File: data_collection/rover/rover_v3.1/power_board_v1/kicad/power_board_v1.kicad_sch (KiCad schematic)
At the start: 96 parts, among them J1 XT60_BATT, J10 from Pi USB2, J11 UPDI prog (UPDI/3V3/GND), J12 XT30 fallback pads, J2 PANEL_SW, J3 USB-C PWR OUT (TH shell), J4 USB_A radio1, J5 USB_A radio2, J6 AUX 5V 2A, J7 PI GPIO harness, J8 AUX_CTL out (JST-GH), J9 from Pi USB1, Q2 SQJQ140E-A diode, Q3 SQJQ140E-B switch, U1 LM25145 5.1V rail A, U2 LM25145 5.1V rail B, U3 ATtiny816, U4 LM74800-Q1, U5 INA226 (addr 0x40), U6 TPS7A16 3V3 60V LDO, U7 TPS2553 1.7A, U8 TPS2553 1.7A, U9 AP2112K-3.3 (switched)

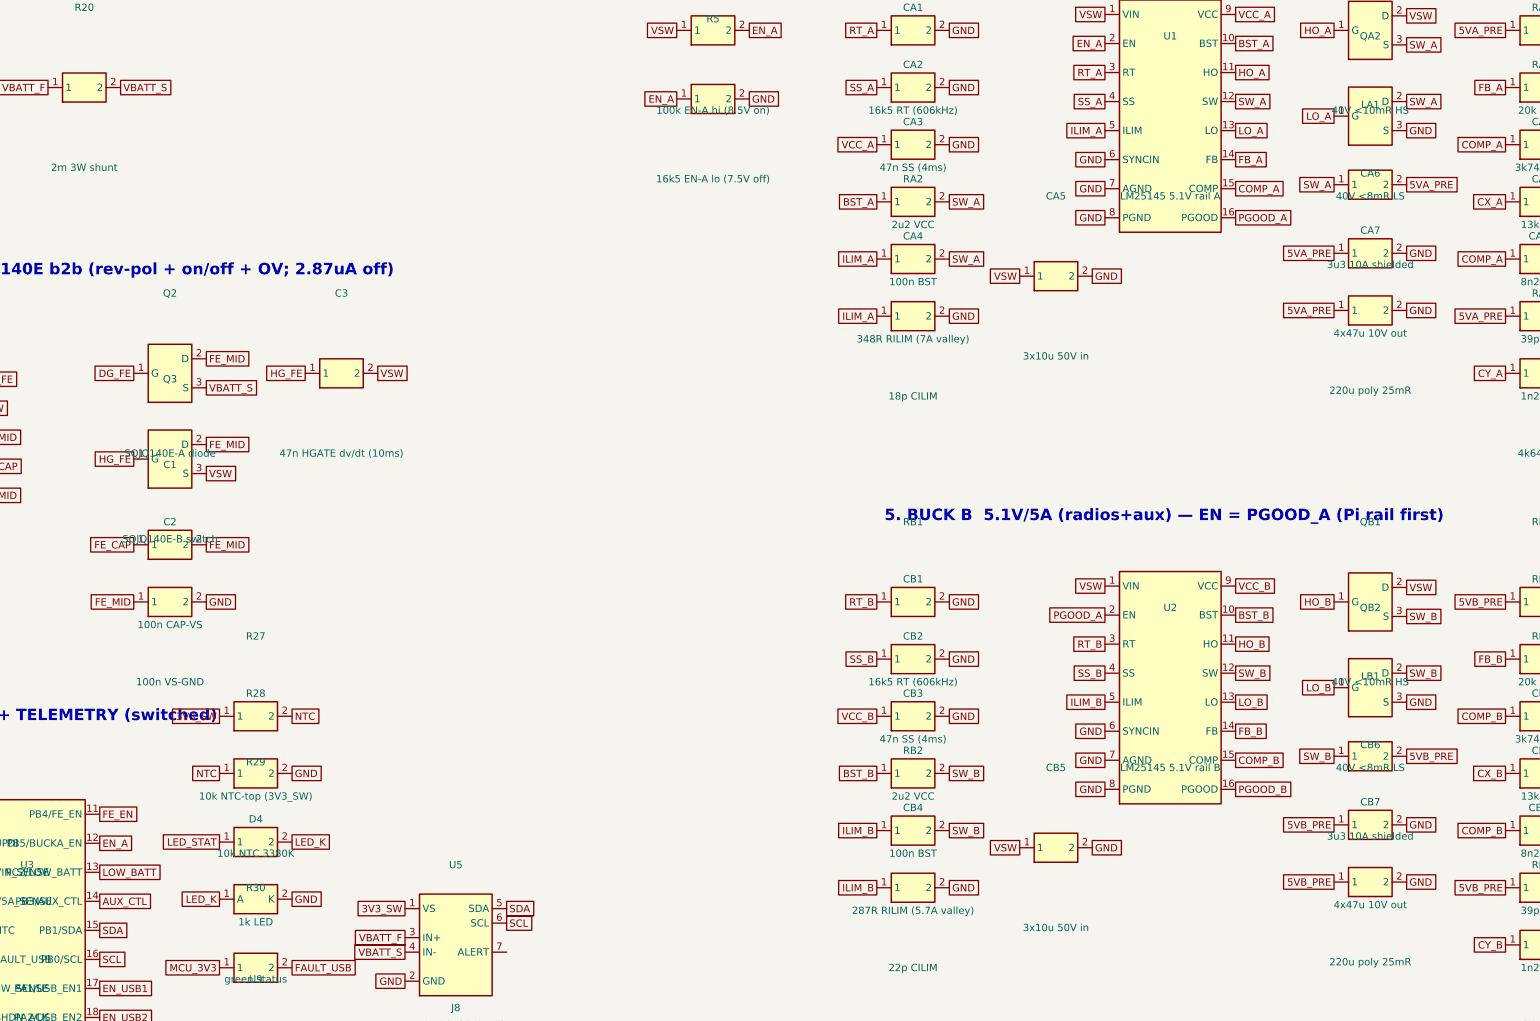
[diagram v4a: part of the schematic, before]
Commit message: P2 BOM lockdown: all lines LCSC-verified w/ C#s; subs LM25145->LM5145 (eq-identical, verified), SQJQ140E->2x CSD18543Q3A, tiny816 SOIC->UQFN; RILIM 301/243; schematic regenerated; ~$43/board @5
Co-Authored-By: Claude Fable 5 <noreply@anthropic.com>
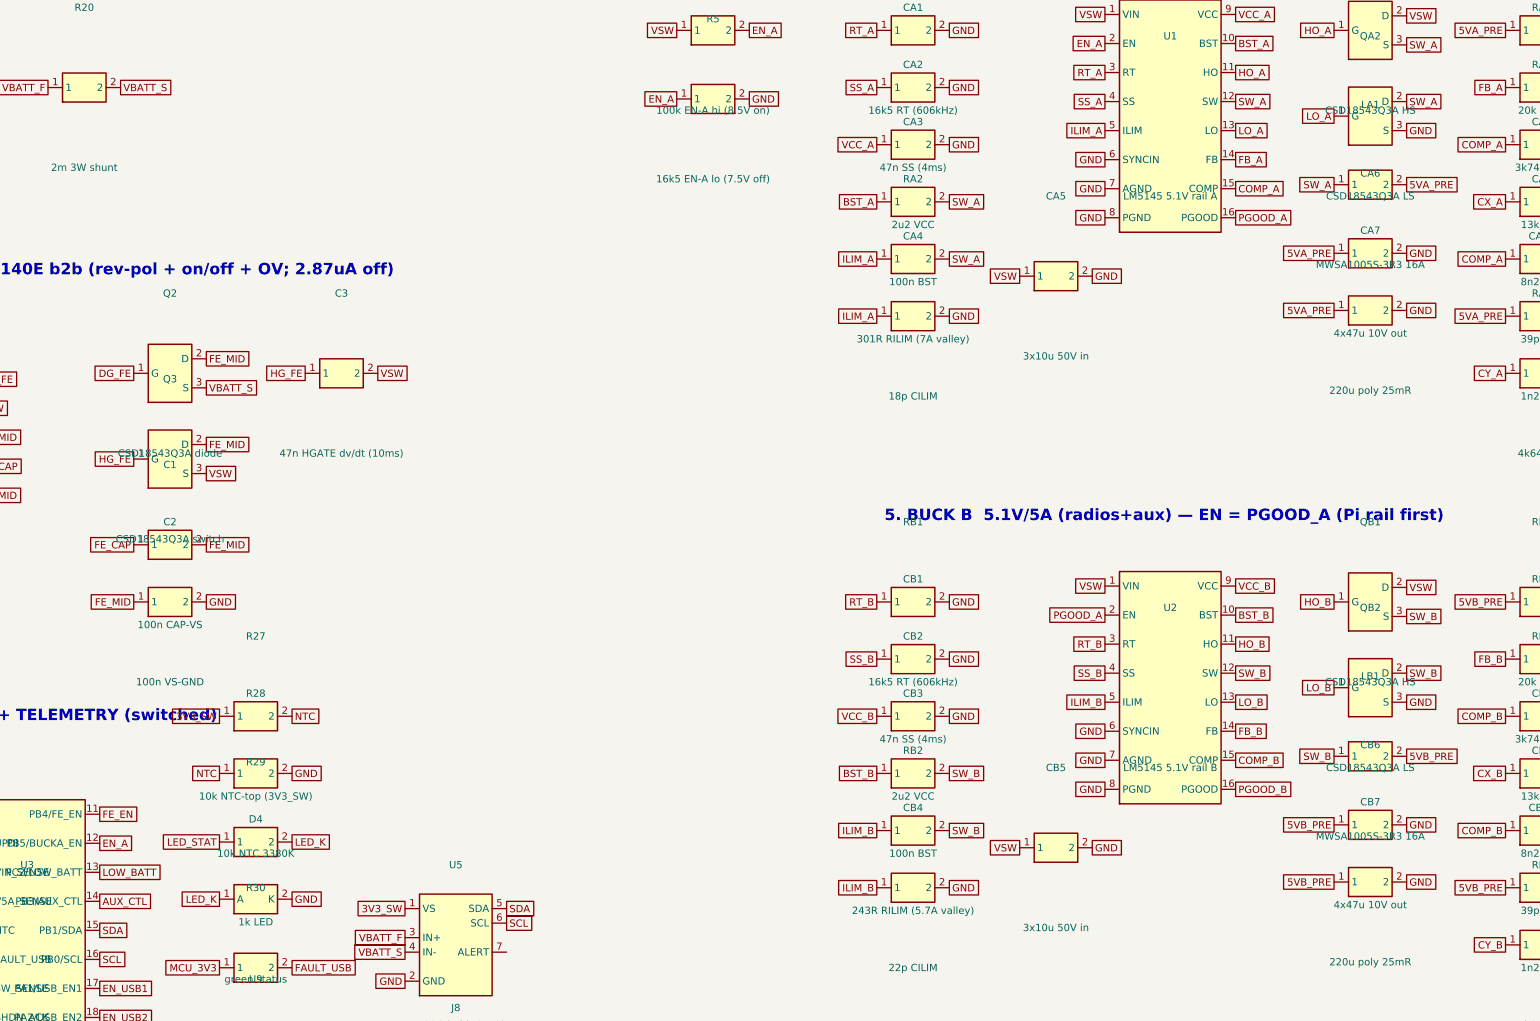
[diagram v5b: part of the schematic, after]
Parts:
- removed U1: LM25145 5.1V rail A, symbol pwr:LM25145
- removed U2: LM25145 5.1V rail B, symbol pwr:LM25145
- added U1: LM5145 5.1V rail A, symbol pwr:LM5145
- added U2: LM5145 5.1V rail B, symbol pwr:LM5145
- LA1, LB1: value 3u3 10A shielded -> MWSA1005S-3R3 16A
- Q2: value SQJQ140E-A diode -> CSD18543Q3A diode
- Q3: value SQJQ140E-B switch -> CSD18543Q3A switch
- QA1, QB1: value 40V <10mR HS -> CSD18543Q3A HS
- QA2, QB2: value 40V <8mR LS -> CSD18543Q3A LS
- RA2: value 348R RILIM (7A valley) -> 301R RILIM (7A valley)
- RB2: value 287R RILIM (5.7A valley) -> 243R RILIM (5.7A valley)
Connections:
- net BST_A: now also U1.10 (BST)
- net BST_B: now also U2.10 (BST)
- net COMP_A: now also U1.15 (COMP)
- net COMP_B: now also U2.15 (COMP)
- net EN_A: now also U1.2 (EN)
- net FB_A: now also U1.14 (FB)
- net FB_B: now also U2.14 (FB)
- net GND: now also U1.6 (SYNCIN), U1.7 (AGND), U1.8 (PGND), U2.6 (SYNCIN), U2.7 (AGND), U2.8 (PGND)
- net HO_A: now also U1.11 (HO)
- net HO_B: now also U2.11 (HO)
- net ILIM_A: now also U1.5 (ILIM)
- net ILIM_B: now also U2.5 (ILIM)
- net LO_A: now also U1.13 (LO)
- net LO_B: now also U2.13 (LO)
- net PGOOD_A: now also U1.16 (PGOOD), U2.2 (EN)
- net PGOOD_B: now also U2.16 (PGOOD)
- net RT_A: now also U1.3 (RT)
- net RT_B: now also U2.3 (RT)
- net SS_A: now also U1.4 (SS)
- net SS_B: now also U2.4 (SS)
- net SW_A: now also U1.12 (SW)
- net SW_B: now also U2.12 (SW)
- net VCC_A: now also U1.9 (VCC)
- net VCC_B: now also U2.9 (VCC)
- net VSW: now also U1.1 (VIN), U2.1 (VIN)

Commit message: P3 prep: FOOTPRINTS.md (land patterns + 90x65 floorplan zones); KiCad-7 dialect emit; schematic PDF export + PNG-verified collision fixes (per-height ref/value offsets, ATtiny width, stale SQJQ140E title); netlist audit clean (73 nets)
Co-Authored-By: Claude Fable 5 <noreply@anthropic.com>
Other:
- note added: "2. FRONT-END: LM74800-Q1 + 2x CSD18543Q3A b2b (rev-pol + on/off + OV; 2.87uA off)"
- note removed: "2. FRONT-END: LM74800-Q1 + SQJQ140E b2b (rev-pol + on/off + OV; 2.87uA off)"

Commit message: Schematic v3: physical package pads throughout (datasheet-verified pinouts for LM5145 RGY, ATtiny816 VQFN, INA226, TPS2553, TPS7A16, AP2112K, CSD18543Q3A); netlist 86 nets clean; 18 pad spot-checks pass; PNG-verified
Co-Authored-By: Claude Fable 5 <noreply@anthropic.com>
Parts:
- removed Q2: CSD18543Q3A diode, symbol pwr:NFET
- removed Q3: CSD18543Q3A switch, symbol pwr:NFET
- removed QA1, QB1: CSD18543Q3A HS, symbol pwr:NFET
- removed QA2, QB2: CSD18543Q3A LS, symbol pwr:NFET
- removed U6: TPS7A16 3V3 60V LDO, symbol pwr:LDO
- removed U9: AP2112K-3.3 (switched), symbol pwr:LDO
- added Q2: CSD18543Q3A diode, symbol pwr:NFET_SON
- added Q3: CSD18543Q3A switch, symbol pwr:NFET_SON
- added QA1, QB1: CSD18543Q3A HS, symbol pwr:NFET_SON
- added QA2, QB2: CSD18543Q3A LS, symbol pwr:NFET_SON
- added U6: TPS7A1633 3V3 60V LDO, symbol pwr:TPS7A16
- added U9: AP2112K-3.3 (switched), symbol pwr:AP2112
- U3: value ATtiny816 -> ATtiny816 (VQFN)
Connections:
- net 3V3_SW: now also U5.6 (VS), U9.5 (VOUT); no longer U5.1 (VS)
- net 5V_B: now also U9.1 (VIN), U9.3 (EN)
- net AUX_CTL: now also U3.11 (PB3/AUX_CTL); no longer U3.14 (PB3/AUX_CTL)
- net BST_A: now also U1.17 (BST); no longer U1.10 (BST)
- net BST_B: now also U2.17 (BST); no longer U2.10 (BST)
- net COMP_A: now also U1.4 (COMP); no longer U1.15 (COMP)
- net COMP_B: now also U2.4 (COMP); no longer U2.15 (COMP)
- net DG_FE: now also Q2.4 (G)
- net EN_A: now also U1.1 (EN), U3.9 (PB5/BUCKA_EN); no longer U1.2 (EN), U3.12 (PB5/BUCKA_EN)
- net EN_USB1: now also U3.20 (PA1/USB_EN1), U7.3 (EN); no longer U3.17 (PA1/USB_EN1), U7.2 (EN)
- net EN_USB2: now also U3.1 (PA2/USB_EN2), U8.3 (EN); no longer U3.18 (PA2/USB_EN2), U8.2 (EN)
- net FAULT_USB: now also U3.6 (PA5/FAULT_USB), U7.4 (FAULT), U8.4 (FAULT); no longer U3.7 (PA5/FAULT_USB), U7.5 (FAULT), U8.5 (FAULT)
- net FB_A: now also U1.5 (FB); no longer U1.14 (FB)
- net FB_B: now also U2.5 (FB); no longer U2.14 (FB)
- net FE_EN: now also U3.10 (PB4/FE_EN); no longer U3.11 (PB4/FE_EN)
- net FE_MID: now also Q2.5 (D), Q2.6 (D), Q2.7 (D), Q2.8 (D), Q3.5 (D), Q3.6 (D), Q3.7 (D), Q3.8 (D)
- net GND: now also U1.12 (PGND), U1.21 (EP), U2.12 (PGND), U2.21 (EP), U3.3 (GND), U5.1 (A1), U5.7 (GND), U7.2 (GND), U8.2 (GND), QA2.1 (S), QA2.2 (S), QA2.3 (S), QB2.1 (S), QB2.2 (S), QB2.3 (S), U6.4 (GND), U6.9 (PAD), U9.2 (GND); no longer U1.7 (AGND), U2.7 (AGND), U3.2 (GND), U7.3 (GND), U8.3 (GND)
- net HG_FE: now also Q3.4 (G)
- net HO_A: now also U1.18 (HO), QA1.4 (G); no longer U1.11 (HO)
- net HO_B: now also U2.18 (HO), QB1.4 (G); no longer U2.11 (HO)
- net ILIM1: now also U7.5 (ILIM); no longer U7.6 (ILIM)
- net ILIM2: now also U8.5 (ILIM); no longer U8.6 (ILIM)
- net ILIM_A: now also U1.11 (ILIM); no longer U1.5 (ILIM)
- net ILIM_B: now also U2.11 (ILIM); no longer U2.5 (ILIM)
- net LED_STAT: now also U3.2 (PA3/LED); no longer U3.19 (PA3/LED)
- net LOW_BATT: now also U3.17 (PC2/LOW_BATT); no longer U3.13 (PC2/LOW_BATT)
- net LO_A: now also QA2.4 (G)
- net LO_B: now also QB2.4 (G)
- net MCU_3V3: now also U3.4 (VDD), U6.1 (OUT); no longer U3.1 (VCC)
- net NTC: now also U3.8 (PA7/NTC); no longer U3.6 (PA7/NTC)
- net PGOOD_A: now also U1.10 (PGOOD), U2.1 (EN), U3.15 (PC0/PGOOD_A); no longer U1.16 (PGOOD), U2.2 (EN), U3.10 (PC0/PGOOD_A)
- net PGOOD_B: now also U2.10 (PGOOD), U3.16 (PC1/PGOOD_B); no longer U2.16 (PGOOD), U3.20 (PC1/PGOOD_B)
- net RT_A: now also U1.2 (RT); no longer U1.3 (RT)
- net RT_B: now also U2.2 (RT); no longer U2.3 (RT)
- net SCL: now also U3.14 (PB0/SCL), U5.5 (SCL); no longer U3.16 (PB0/SCL), U5.6 (SCL)
- net SDA: now also U3.13 (PB1/SDA), U5.4 (SDA); no longer U3.15 (PB1/SDA), U5.5 (SDA)
- net SHDN_ACK: now also U3.18 (PC3/SHDN_ACK); no longer U3.9 (PC3/SHDN_ACK)
- net SS_A: now also U1.3 (SS); no longer U1.4 (SS)
- net SS_B: now also U2.3 (SS); no longer U2.4 (SS)
- net SW_A: now also U1.19 (SW), QA1.1 (S), QA1.2 (S), QA1.3 (S), QA2.5 (D), QA2.6 (D), QA2.7 (D), QA2.8 (D); no longer U1.12 (SW)
- net SW_B: now also U2.19 (SW), QB1.1 (S), QB1.2 (S), QB1.3 (S), QB2.5 (D), QB2.6 (D), QB2.7 (D), QB2.8 (D); no longer U2.12 (SW)
- net SW_SENSE: now also U3.12 (PB2/SW_SENSE); no longer U3.8 (PB2/SW_SENSE)
- net UPDI: now also U3.19 (PA0/UPDI); no longer U3.3 (PA0/UPDI)
- net V5A_SENSE: now also U3.7 (PA6/V5A_SENSE); no longer U3.5 (PA6/V5A_SENSE)
- net VBATT_F: now also U5.10 (IN+), U6.5 (EN), U6.8 (IN); no longer U5.3 (IN+)
- net VBATT_S: now also U5.8 (VBUS), U5.9 (IN-), Q2.1 (S), Q2.2 (S), Q2.3 (S); no longer U5.4 (IN-)
- net VBUS1: now also U7.6 (OUT); no longer U7.4 (OUT)
- net VBUS2: now also U8.6 (OUT); no longer U8.4 (OUT)
- net VCC_A: now also U1.14 (VCC); no longer U1.9 (VCC)
- net VCC_B: now also U2.14 (VCC); no longer U2.9 (VCC)
- net VSENSE: now also U3.5 (PA4/VIN_SENSE); no longer U3.4 (PA4/VIN_SENSE)
- net VSW: now also U1.20 (VIN), U2.20 (VIN), Q3.1 (S), Q3.2 (S), Q3.3 (S), QA1.5 (D), QA1.6 (D), QA1.7 (D), QA1.8 (D), QB1.5 (D), QB1.6 (D), QB1.7 (D), QB1.8 (D); no longer U1.1 (VIN), U2.1 (VIN)
